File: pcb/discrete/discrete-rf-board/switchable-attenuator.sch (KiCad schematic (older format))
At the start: 11 parts, among them U18 BGS12PL6E6327XTSA1, U19 BGS12PL6E6327XTSA1

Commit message: Autofill
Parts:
- C192, C195: footprint (none) -> Capacitor_SMD:C_0402_1005Metric; Mouser (none) -> 80-C0402C103K4R7411
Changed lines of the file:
@@
 F 0 "C198" H 4910 2220 50  0000 L CNN
 F 1 "0.01 uF" H 4910 2070 50  0000 L CNN
-F 2 "" H 4900 2150 50  0001 C CNN
+F 2 "Capacitor_SMD:C_0402_1005Metric" H 4900 2150 50  0001 C CNN
 F 3 "~" H 4900 2150 50  0001 C CNN
+F 4 "80-C0402C103K4R7411" H 4900 2150 50  0001 C CNN "Mouser"
 	1    4900 2150
 	1    0    0    -1
@@
 F 0 "C201" H 6960 2270 50  0000 L CNN
 F 1 "0.01 uF" H 6960 2120 50  0000 L CNN
-F 2 "" H 6950 2200 50  0001 C CNN
+F 2 "Capacitor_SMD:C_0402_1005Metric" H 6950 2200 50  0001 C CNN
 F 3 "~" H 6950 2200 50  0001 C CNN
+F 4 "80-C0402C103K4R7411" H 6950 2200 50  0001 C CNN "Mouser"
 	1    6950 2200
 	1    0    0    -1

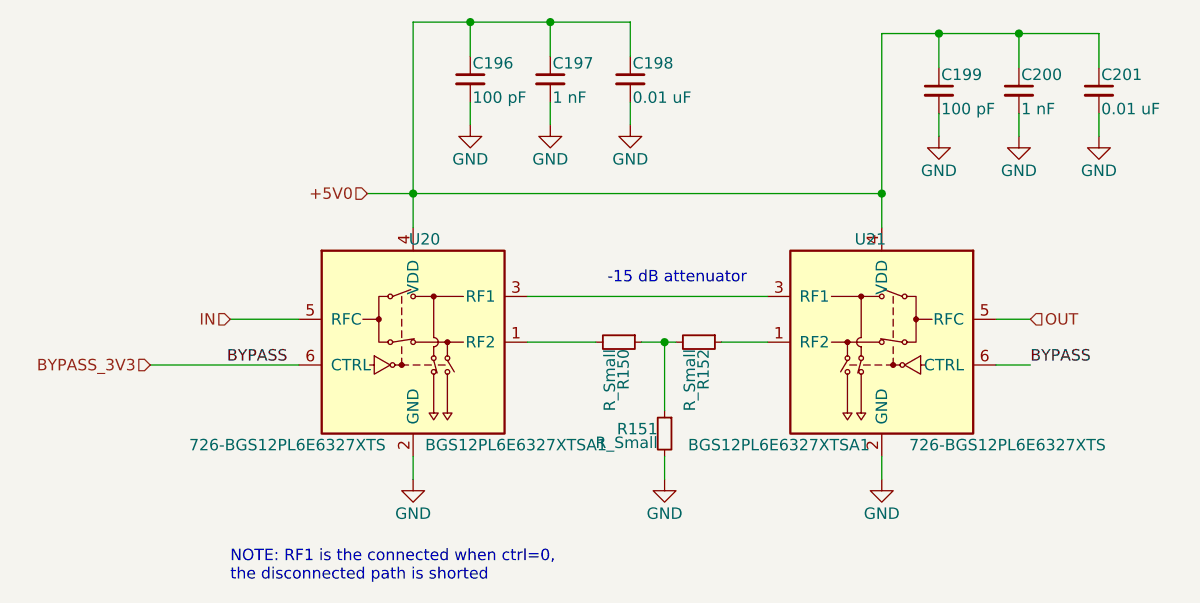
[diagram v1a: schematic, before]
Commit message: Reannotate everything; I'm trying to cut down the number of components
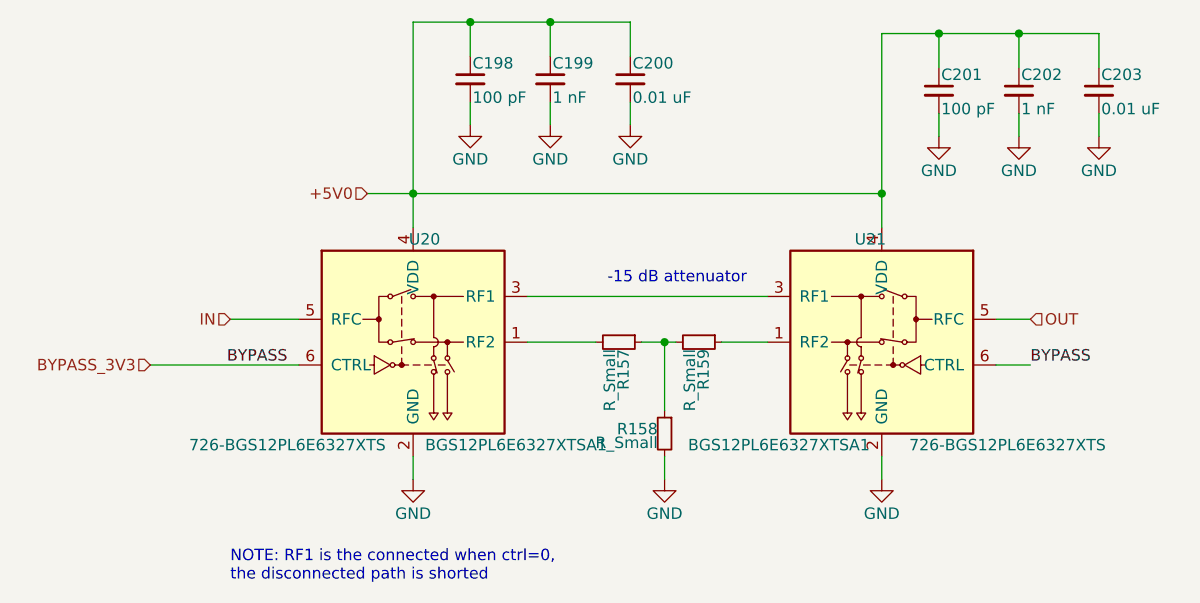
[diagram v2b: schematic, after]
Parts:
- renumbered C190 to C192, C191 to C193, C192 to C194, C193 to C195, C194 to C196, C195 to C197, R147 to R154, R148 to R155, R149 to R156
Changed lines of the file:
@@
 P 4850 3300
 AR Path="/5CA6B0AA/5CE74EBE/5D4B1FCA" Ref="R?"  Part="1"
-AR Path="/5CA6B0AA/5CE74EBE/5D4B0AA8/5D4B1FCA" Ref="R147"  Part="1"
-AR Path="/5CA6B0AA/5CE74EBE/5D4C7749/5D4B1FCA" Ref="R150"  Part="1"
-F 0 "R150" H 4880 3320 50  0000 L CNN
+AR Path="/5CA6B0AA/5CE74EBE/5D4B0AA8/5D4B1FCA" Ref="R154"  Part="1"
+AR Path="/5CA6B0AA/5CE74EBE/5D4C7749/5D4B1FCA" Ref="R157"  Part="1"
+F 0 "R157" H 4880 3320 50  0000 L CNN
 F 1 "R_Small" H 4880 3260 50  0000 L CNN
 F 2 "" H 4850 3300 50  0001 C CNN
@@
 P 5200 3300
 AR Path="/5CA6B0AA/5CE74EBE/5D4B1FD0" Ref="R?"  Part="1"
-AR Path="/5CA6B0AA/5CE74EBE/5D4B0AA8/5D4B1FD0" Ref="R149"  Part="1"
-AR Path="/5CA6B0AA/5CE74EBE/5D4C7749/5D4B1FD0" Ref="R152"  Part="1"
-F 0 "R152" H 5230 3320 50  0000 L CNN
+AR Path="/5CA6B0AA/5CE74EBE/5D4B0AA8/5D4B1FD0" Ref="R156"  Part="1"
+AR Path="/5CA6B0AA/5CE74EBE/5D4C7749/5D4B1FD0" Ref="R159"  Part="1"
+F 0 "R159" H 5230 3320 50  0000 L CNN
 F 1 "R_Small" H 5230 3260 50  0000 L CNN
 F 2 "" H 5200 3300 50  0001 C CNN
@@
 P 5050 3700
 AR Path="/5CA6B0AA/5CE74EBE/5D4B1FD6" Ref="R?"  Part="1"
-AR Path="/5CA6B0AA/5CE74EBE/5D4B0AA8/5D4B1FD6" Ref="R148"  Part="1"
-AR Path="/5CA6B0AA/5CE74EBE/5D4C7749/5D4B1FD6" Ref="R151"  Part="1"
-F 0 "R151" H 5080 3720 50  0000 L CNN
+AR Path="/5CA6B0AA/5CE74EBE/5D4B0AA8/5D4B1FD6" Ref="R155"  Part="1"
+AR Path="/5CA6B0AA/5CE74EBE/5D4C7749/5D4B1FD6" Ref="R158"  Part="1"
+F 0 "R158" H 5080 3720 50  0000 L CNN
 F 1 "R_Small" H 5080 3660 50  0000 L CNN
 F 2 "" H 5050 3700 50  0001 C CNN
@@
 	3950 2650 6000 2650
 $Comp
-L Device:C_Small C190
+L Device:C_Small C192
 U 1 1 5D4BC42E
 P 4200 2150
-AR Path="/5CA6B0AA/5CE74EBE/5D4B0AA8/5D4BC42E" Ref="C190"  Part="1"
-AR Path="/5CA6B0AA/5CE74EBE/5D4C7749/5D4BC42E" Ref="C196"  Part="1"
-F 0 "C196" H 4210 2220 50  0000 L CNN
+AR Path="/5CA6B0AA/5CE74EBE/5D4B0AA8/5D4BC42E" Ref="C192"  Part="1"
+AR Path="/5CA6B0AA/5CE74EBE/5D4C7749/5D4BC42E" Ref="C198"  Part="1"
+F 0 "C198" H 4210 2220 50  0000 L CNN
 F 1 "100 pF" H 4210 2070 50  0000 L CNN
 F 2 "Capacitor_SMD:C_0402_1005Metric" H 4200 2150 50  0001 C CNN
@@
 $EndComp
 $Comp
-L Device:C_Small C191
+L Device:C_Small C193
 U 1 1 5D4BC853
 P 4550 2150
-AR Path="/5CA6B0AA/5CE74EBE/5D4B0AA8/5D4BC853" Ref="C191"  Part="1"
-AR Path="/5CA6B0AA/5CE74EBE/5D4C7749/5D4BC853" Ref="C197"  Part="1"
-F 0 "C197" H 4560 2220 50  0000 L CNN
+AR Path="/5CA6B0AA/5CE74EBE/5D4B0AA8/5D4BC853" Ref="C193"  Part="1"
+AR Path="/5CA6B0AA/5CE74EBE/5D4C7749/5D4BC853" Ref="C199"  Part="1"
+F 0 "C199" H 4560 2220 50  0000 L CNN
 F 1 "1 nF" H 4560 2070 50  0000 L CNN
 F 2 "" H 4550 2150 50  0001 C CNN
@@
 $EndComp
 $Comp
-L Device:C_Small C192
+L Device:C_Small C194
 U 1 1 5D4BCC70
 P 4900 2150
-AR Path="/5CA6B0AA/5CE74EBE/5D4B0AA8/5D4BCC70" Ref="C192"  Part="1"
-AR Path="/5CA6B0AA/5CE74EBE/5D4C7749/5D4BCC70" Ref="C198"  Part="1"
-F 0 "C198" H 4910 2220 50  0000 L CNN
+AR Path="/5CA6B0AA/5CE74EBE/5D4B0AA8/5D4BCC70" Ref="C194"  Part="1"
+AR Path="/5CA6B0AA/5CE74EBE/5D4C7749/5D4BCC70" Ref="C200"  Part="1"
+F 0 "C200" H 4910 2220 50  0000 L CNN
 F 1 "0.01 uF" H 4910 2070 50  0000 L CNN
 F 2 "Capacitor_SMD:C_0402_1005Metric" H 4900 2150 50  0001 C CNN
@@
 $EndComp
 $Comp
-L Device:C_Small C193
+L Device:C_Small C195
 U 1 1 5D4BED00
 P 6250 2200
-AR Path="/5CA6B0AA/5CE74EBE/5D4B0AA8/5D4BED00" Ref="C193"  Part="1"
-AR Path="/5CA6B0AA/5CE74EBE/5D4C7749/5D4BED00" Ref="C199"  Part="1"
-F 0 "C199" H 6260 2270 50  0000 L CNN
+AR Path="/5CA6B0AA/5CE74EBE/5D4B0AA8/5D4BED00" Ref="C195"  Part="1"
+AR Path="/5CA6B0AA/5CE74EBE/5D4C7749/5D4BED00" Ref="C201"  Part="1"
+F 0 "C201" H 6260 2270 50  0000 L CNN
 F 1 "100 pF" H 6260 2120 50  0000 L CNN
 F 2 "Capacitor_SMD:C_0402_1005Metric" H 6250 2200 50  0001 C CNN
@@
 $EndComp
 $Comp
-L Device:C_Small C194
+L Device:C_Small C196
 U 1 1 5D4BED06
 P 6600 2200
-AR Path="/5CA6B0AA/5CE74EBE/5D4B0AA8/5D4BED06" Ref="C194"  Part="1"
-AR Path="/5CA6B0AA/5CE74EBE/5D4C7749/5D4BED06" Ref="C200"  Part="1"
-F 0 "C200" H 6610 2270 50  0000 L CNN
+AR Path="/5CA6B0AA/5CE74EBE/5D4B0AA8/5D4BED06" Ref="C196"  Part="1"
+AR Path="/5CA6B0AA/5CE74EBE/5D4C7749/5D4BED06" Ref="C202"  Part="1"
+F 0 "C202" H 6610 2270 50  0000 L CNN
 F 1 "1 nF" H 6610 2120 50  0000 L CNN
 F 2 "" H 6600 2200 50  0001 C CNN
@@
 $EndComp
 $Comp
-L Device:C_Small C195
+L Device:C_Small C197
 U 1 1 5D4BED0C
 P 6950 2200
-AR Path="/5CA6B0AA/5CE74EBE/5D4B0AA8/5D4BED0C" Ref="C195"  Part="1"
-AR Path="/5CA6B0AA/5CE74EBE/5D4C7749/5D4BED0C" Ref="C201"  Part="1"
-F 0 "C201" H 6960 2270 50  0000 L CNN
+AR Path="/5CA6B0AA/5CE74EBE/5D4B0AA8/5D4BED0C" Ref="C197"  Part="1"
+AR Path="/5CA6B0AA/5CE74EBE/5D4C7749/5D4BED0C" Ref="C203"  Part="1"
+F 0 "C203" H 6960 2270 50  0000 L CNN
 F 1 "0.01 uF" H 6960 2120 50  0000 L CNN
 F 2 "Capacitor_SMD:C_0402_1005Metric" H 6950 2200 50  0001 C CNN

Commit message: Autofill
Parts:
- C193, C196: footprint (none) -> Capacitor_SMD:C_0402_1005Metric; Mouser (none) -> 80-C0402C102K5R7411
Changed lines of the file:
@@
 F 0 "C199" H 4560 2220 50  0000 L CNN
 F 1 "1 nF" H 4560 2070 50  0000 L CNN
-F 2 "" H 4550 2150 50  0001 C CNN
+F 2 "Capacitor_SMD:C_0402_1005Metric" H 4550 2150 50  0001 C CNN
 F 3 "~" H 4550 2150 50  0001 C CNN
+F 4 "80-C0402C102K5R7411" H 4550 2150 50  0001 C CNN "Mouser"
 	1    4550 2150
 	1    0    0    -1
@@
 F 0 "C202" H 6610 2270 50  0000 L CNN
 F 1 "1 nF" H 6610 2120 50  0000 L CNN
-F 2 "" H 6600 2200 50  0001 C CNN
+F 2 "Capacitor_SMD:C_0402_1005Metric" H 6600 2200 50  0001 C CNN
 F 3 "~" H 6600 2200 50  0001 C CNN
+F 4 "80-C0402C102K5R7411" H 6600 2200 50  0001 C CNN "Mouser"
 	1    6600 2200
 	1    0    0    -1

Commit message: Footprint more stuff
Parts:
- R154, R155, R156: value R_Small -> TBD 0402
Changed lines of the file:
@@
 AR Path="/5CA6B0AA/5CE74EBE/5D4B0AA8/5D4B1FC3" Ref="U18"  Part="1"
 AR Path="/5CA6B0AA/5CE74EBE/5D4C7749/5D4B1FC3" Ref="U20"  Part="1"
-F 0 "U20" H 4000 3750 50  0000 C CNN
+F 0 "U18" H 4000 3750 50  0000 C CNN
 F 1 "BGS12PL6E6327XTSA1" H 4400 2850 50  0000 C CNN
 F 2 "discrete_footprints:Infineon_TSLP-6-4" H 3950 3300 50  0001 C CNN
@@
 AR Path="/5CA6B0AA/5CE74EBE/5D4B0AA8/5D4B1FCA" Ref="R154"  Part="1"
 AR Path="/5CA6B0AA/5CE74EBE/5D4C7749/5D4B1FCA" Ref="R157"  Part="1"
-F 0 "R157" H 4880 3320 50  0000 L CNN
-F 1 "R_Small" H 4880 3260 50  0000 L CNN
+F 0 "R154" H 4880 3320 50  0000 L CNN
+F 1 "TBD 0402" H 4880 3260 50  0000 L CNN
 F 2 "" H 4850 3300 50  0001 C CNN
 F 3 "~" H 4850 3300 50  0001 C CNN
@@
 AR Path="/5CA6B0AA/5CE74EBE/5D4B0AA8/5D4B1FD0" Ref="R156"  Part="1"
 AR Path="/5CA6B0AA/5CE74EBE/5D4C7749/5D4B1FD0" Ref="R159"  Part="1"
-F 0 "R159" H 5230 3320 50  0000 L CNN
-F 1 "R_Small" H 5230 3260 50  0000 L CNN
+F 0 "R156" H 5230 3320 50  0000 L CNN
+F 1 "TBD 0402" H 5230 3260 50  0000 L CNN
 F 2 "" H 5200 3300 50  0001 C CNN
 F 3 "~" H 5200 3300 50  0001 C CNN
@@
 AR Path="/5CA6B0AA/5CE74EBE/5D4B0AA8/5D4B1FD6" Ref="R155"  Part="1"
 AR Path="/5CA6B0AA/5CE74EBE/5D4C7749/5D4B1FD6" Ref="R158"  Part="1"
-F 0 "R158" H 5080 3720 50  0000 L CNN
-F 1 "R_Small" H 5080 3660 50  0000 L CNN
+F 0 "R155" H 5080 3720 50  0000 L CNN
+F 1 "TBD 0402" H 5080 3660 50  0000 L CNN
 F 2 "" H 5050 3700 50  0001 C CNN
 F 3 "~" H 5050 3700 50  0001 C CNN
@@
 AR Path="/5CA6B0AA/5CE74EBE/5D4B0AA8/5D4B1FDD" Ref="#PWR0238"  Part="1"
 AR Path="/5CA6B0AA/5CE74EBE/5D4C7749/5D4B1FDD" Ref="#PWR0247"  Part="1"
-F 0 "#PWR0247" H 3950 3650 50  0001 C CNN
+F 0 "#PWR0238" H 3950 3650 50  0001 C CNN
 F 1 "GND" H 3950 3750 50  0000 C CNN
 F 2 "" H 3950 3900 50  0001 C CNN
@@
 AR Path="/5CA6B0AA/5CE74EBE/5D4B0AA8/5D4B1FE5" Ref="#PWR0242"  Part="1"
 AR Path="/5CA6B0AA/5CE74EBE/5D4C7749/5D4B1FE5" Ref="#PWR0251"  Part="1"
-F 0 "#PWR0251" H 5050 3650 50  0001 C CNN
+F 0 "#PWR0242" H 5050 3650 50  0001 C CNN
 F 1 "GND" H 5050 3750 50  0000 C CNN
 F 2 "" H 5050 3900 50  0001 C CNN
@@
 AR Path="/5CA6B0AA/5CE74EBE/5D4B0AA8/5D4B2001" Ref="#PWR0243"  Part="1"
 AR Path="/5CA6B0AA/5CE74EBE/5D4C7749/5D4B2001" Ref="#PWR0252"  Part="1"
-F 0 "#PWR0252" H 6000 3650 50  0001 C CNN
+F 0 "#PWR0243" H 6000 3650 50  0001 C CNN
 F 1 "GND" H 6000 3750 50  0000 C CNN
 F 2 "" H 6000 3900 50  0001 C CNN
@@
 AR Path="/5CA6B0AA/5CE74EBE/5D4B0AA8/5D4B1FF8" Ref="U19"  Part="1"
 AR Path="/5CA6B0AA/5CE74EBE/5D4C7749/5D4B1FF8" Ref="U21"  Part="1"
-F 0 "U21" H 6050 3750 50  0000 C CNN
+F 0 "U19" H 6050 3750 50  0000 C CNN
 F 1 "BGS12PL6E6327XTSA1" H 6450 2850 50  0000 C CNN
 F 2 "discrete_footprints:Infineon_TSLP-6-4" H 6000 3300 50  0001 C CNN
@@
 AR Path="/5CA6B0AA/5CE74EBE/5D4B0AA8/5D4BC42E" Ref="C192"  Part="1"
 AR Path="/5CA6B0AA/5CE74EBE/5D4C7749/5D4BC42E" Ref="C198"  Part="1"
-F 0 "C198" H 4210 2220 50  0000 L CNN
+F 0 "C192" H 4210 2220 50  0000 L CNN
 F 1 "100 pF" H 4210 2070 50  0000 L CNN
 F 2 "Capacitor_SMD:C_0402_1005Metric" H 4200 2150 50  0001 C CNN
@@
 AR Path="/5CA6B0AA/5CE74EBE/5D4B0AA8/5D4BC853" Ref="C193"  Part="1"
 AR Path="/5CA6B0AA/5CE74EBE/5D4C7749/5D4BC853" Ref="C199"  Part="1"
-F 0 "C199" H 4560 2220 50  0000 L CNN
+F 0 "C193" H 4560 2220 50  0000 L CNN
 F 1 "1 nF" H 4560 2070 50  0000 L CNN
 F 2 "Capacitor_SMD:C_0402_1005Metric" H 4550 2150 50  0001 C CNN
@@
 AR Path="/5CA6B0AA/5CE74EBE/5D4B0AA8/5D4BCC70" Ref="C194"  Part="1"
 AR Path="/5CA6B0AA/5CE74EBE/5D4C7749/5D4BCC70" Ref="C200"  Part="1"
-F 0 "C200" H 4910 2220 50  0000 L CNN
+F 0 "C194" H 4910 2220 50  0000 L CNN
 F 1 "0.01 uF" H 4910 2070 50  0000 L CNN
 F 2 "Capacitor_SMD:C_0402_1005Metric" H 4900 2150 50  0001 C CNN
@@
 AR Path="/5CA6B0AA/5CE74EBE/5D4B0AA8/5D4BED00" Ref="C195"  Part="1"
 AR Path="/5CA6B0AA/5CE74EBE/5D4C7749/5D4BED00" Ref="C201"  Part="1"
-F 0 "C201" H 6260 2270 50  0000 L CNN
+F 0 "C195" H 6260 2270 50  0000 L CNN
 F 1 "100 pF" H 6260 2120 50  0000 L CNN
 F 2 "Capacitor_SMD:C_0402_1005Metric" H 6250 2200 50  0001 C CNN
@@
 AR Path="/5CA6B0AA/5CE74EBE/5D4B0AA8/5D4BED06" Ref="C196"  Part="1"
 AR Path="/5CA6B0AA/5CE74EBE/5D4C7749/5D4BED06" Ref="C202"  Part="1"
-F 0 "C202" H 6610 2270 50  0000 L CNN
+F 0 "C196" H 6610 2270 50  0000 L CNN
 F 1 "1 nF" H 6610 2120 50  0000 L CNN
 F 2 "Capacitor_SMD:C_0402_1005Metric" H 6600 2200 50  0001 C CNN
@@
 AR Path="/5CA6B0AA/5CE74EBE/5D4B0AA8/5D4BED0C" Ref="C197"  Part="1"
 AR Path="/5CA6B0AA/5CE74EBE/5D4C7749/5D4BED0C" Ref="C203"  Part="1"
-F 0 "C203" H 6960 2270 50  0000 L CNN
+F 0 "C197" H 6960 2270 50  0000 L CNN
 F 1 "0.01 uF" H 6960 2120 50  0000 L CNN
 F 2 "Capacitor_SMD:C_0402_1005Metric" H 6950 2200 50  0001 C CNN
@@
 AR Path="/5CA6B0AA/5CE74EBE/5D4B0AA8/5D4BF277" Ref="#PWR0246"  Part="1"
 AR Path="/5CA6B0AA/5CE74EBE/5D4C7749/5D4BF277" Ref="#PWR0255"  Part="1"
-F 0 "#PWR0255" H 6950 2150 50  0001 C CNN
+F 0 "#PWR0246" H 6950 2150 50  0001 C CNN
 F 1 "GND" H 6950 2250 50  0000 C CNN
 F 2 "" H 6950 2400 50  0001 C CNN
@@
 AR Path="/5CA6B0AA/5CE74EBE/5D4B0AA8/5D4BF7E8" Ref="#PWR0245"  Part="1"
 AR Path="/5CA6B0AA/5CE74EBE/5D4C7749/5D4BF7E8" Ref="#PWR0254"  Part="1"
-F 0 "#PWR0254" H 6600 2150 50  0001 C CNN
+F 0 "#PWR0245" H 6600 2150 50  0001 C CNN
 F 1 "GND" H 6600 2250 50  0000 C CNN
 F 2 "" H 6600 2400 50  0001 C CNN
@@
 AR Path="/5CA6B0AA/5CE74EBE/5D4B0AA8/5D4BFA67" Ref="#PWR0244"  Part="1"
 AR Path="/5CA6B0AA/5CE74EBE/5D4C7749/5D4BFA67" Ref="#PWR0253"  Part="1"
-F 0 "#PWR0253" H 6250 2150 50  0001 C CNN
+F 0 "#PWR0244" H 6250 2150 50  0001 C CNN
 F 1 "GND" H 6250 2250 50  0000 C CNN
 F 2 "" H 6250 2400 50  0001 C CNN
@@
 AR Path="/5CA6B0AA/5CE74EBE/5D4B0AA8/5D4C425B" Ref="#PWR0241"  Part="1"
 AR Path="/5CA6B0AA/5CE74EBE/5D4C7749/5D4C425B" Ref="#PWR0250"  Part="1"
-F 0 "#PWR0250" H 4900 2100 50  0001 C CNN
+F 0 "#PWR0241" H 4900 2100 50  0001 C CNN
 F 1 "GND" H 4900 2200 50  0000 C CNN
 F 2 "" H 4900 2350 50  0001 C CNN
@@
 AR Path="/5CA6B0AA/5CE74EBE/5D4B0AA8/5D4C4261" Ref="#PWR0240"  Part="1"
 AR Path="/5CA6B0AA/5CE74EBE/5D4C7749/5D4C4261" Ref="#PWR0249"  Part="1"
-F 0 "#PWR0249" H 4550 2100 50  0001 C CNN
+F 0 "#PWR0240" H 4550 2100 50  0001 C CNN
 F 1 "GND" H 4550 2200 50  0000 C CNN
 F 2 "" H 4550 2350 50  0001 C CNN
@@
 AR Path="/5CA6B0AA/5CE74EBE/5D4B0AA8/5D4C4267" Ref="#PWR0239"  Part="1"
 AR Path="/5CA6B0AA/5CE74EBE/5D4C7749/5D4C4267" Ref="#PWR0248"  Part="1"
-F 0 "#PWR0248" H 4200 2100 50  0001 C CNN
+F 0 "#PWR0239" H 4200 2100 50  0001 C CNN
 F 1 "GND" H 4200 2200 50  0000 C CNN
 F 2 "" H 4200 2350 50  0001 C CNN

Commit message: Autofill
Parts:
- R154, R155, R156: footprint (none) -> Resistor_SMD:R_0402_1005Metric; Mouser (none) -> NoPart
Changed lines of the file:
@@
 F 0 "R154" H 4880 3320 50  0000 L CNN
 F 1 "TBD 0402" H 4880 3260 50  0000 L CNN
-F 2 "" H 4850 3300 50  0001 C CNN
+F 2 "Resistor_SMD:R_0402_1005Metric" H 4850 3300 50  0001 C CNN
 F 3 "~" H 4850 3300 50  0001 C CNN
+F 4 "NoPart" H 4850 3300 50  0001 C CNN "Mouser"
 	1    4850 3300
 	0    1    1    0
@@
 F 0 "R156" H 5230 3320 50  0000 L CNN
 F 1 "TBD 0402" H 5230 3260 50  0000 L CNN
-F 2 "" H 5200 3300 50  0001 C CNN
+F 2 "Resistor_SMD:R_0402_1005Metric" H 5200 3300 50  0001 C CNN
 F 3 "~" H 5200 3300 50  0001 C CNN
+F 4 "NoPart" H 5200 3300 50  0001 C CNN "Mouser"
 	1    5200 3300
 	0    1    1    0
@@
 F 0 "R155" H 5080 3720 50  0000 L CNN
 F 1 "TBD 0402" H 5080 3660 50  0000 L CNN
-F 2 "" H 5050 3700 50  0001 C CNN
+F 2 "Resistor_SMD:R_0402_1005Metric" H 5050 3700 50  0001 C CNN
 F 3 "~" H 5050 3700 50  0001 C CNN
+F 4 "NoPart" H 5050 3700 50  0001 C CNN "Mouser"
 	1    5050 3700
 	-1   0    0    -1
